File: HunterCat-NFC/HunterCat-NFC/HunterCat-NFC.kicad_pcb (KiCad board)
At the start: 2 copper layers, 80.7 x 33.5 mm, 64 parts, among them J1 Battery, J2 Conn_01x06_Female, P1 USB_C_Plug_USB2.0, Q1 DMG3415U-7, SW1 RESET, SW2 GPIO, SW3 GPIO1, SW4 GPIO2, U1 ATSAMD21E18A, U2 PN7150B0HN_C11002E-PN7150B0HN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

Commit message: add logos and mounitng holes again
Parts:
- added G***: LOGO, Aesthetics:electronic_cats_logo_4x3, F.Cu at (127.3, 105.0)
- added G***: LOGO, Aesthetics:electronic_cats_logo_4x3, B.Cu at (91.2, 92.2)
- added H1: MountingHole, MountingHole:MountingHole_2.2mm_M2, F.Cu at (83.0, 78.4)
- added H2: MountingHole, MountingHole:MountingHole_2.2mm_M2, F.Cu at (83.0, 106.1)
- added H3: MountingHole, MountingHole:MountingHole_2.2mm_M2, F.Cu at (155.8, 78.1)
- added H4: MountingHole, MountingHole:MountingHole_2.2mm_M2, F.Cu at (156.2, 106.5)

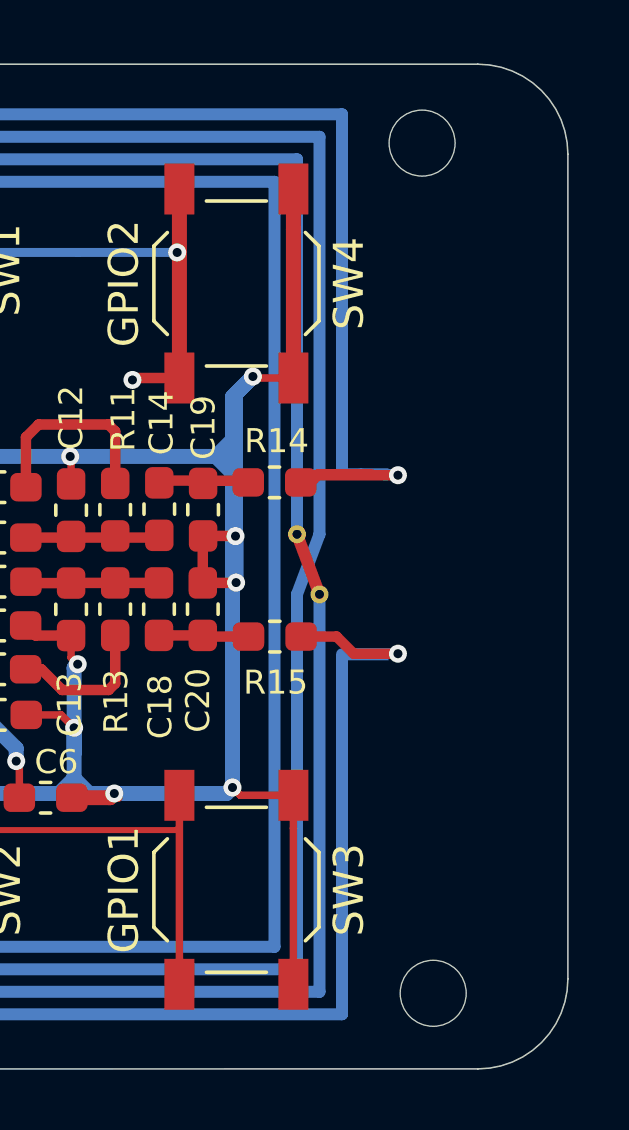
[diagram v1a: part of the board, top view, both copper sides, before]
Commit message: Accommodated screw holes
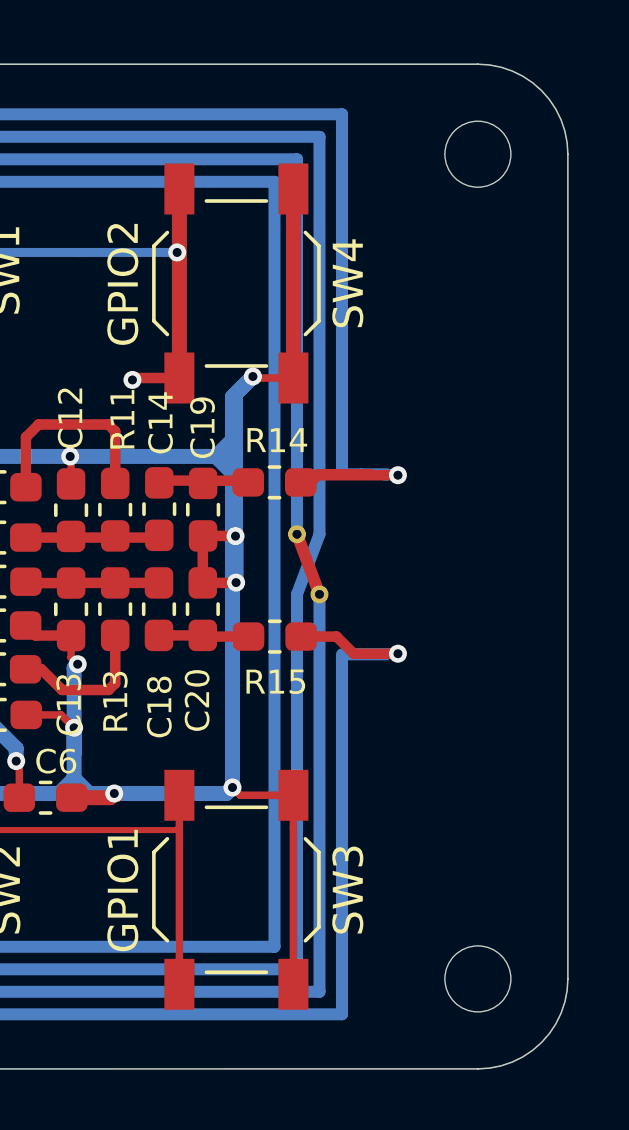
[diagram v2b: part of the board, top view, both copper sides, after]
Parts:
- moved H3 1.90 mm to (157.7, 78.5)
- moved H4 1.57 mm to (157.7, 106.0)
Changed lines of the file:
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@@
-(kicad_pcb (version 20171130) (host pcbnew "(5.1.5-0-10_14)")
+(kicad_pcb (version 20171130) (host pcbnew "(5.1.5)-3")
   (general
     (thickness 1.6)
@@
   )
   (layers
-    (0 F.Cu signal hide)
-    (31 B.Cu signal hide)
+    (0 F.Cu signal)
+    (31 B.Cu signal)
     (32 B.Adhes user)
     (33 F.Adhes user)
@@
   )
   (module MountingHole:MountingHole_2.2mm_M2 (layer F.Cu)
-    (at 156.2 106.47)
+    (at 157.69 105.99)
     (descr "Mounting Hole 2.2mm, no annular, M2")
     (tags "mounting hole 2.2mm no annular m2")
@@
   )
   (module MountingHole:MountingHole_2.2mm_M2 (layer F.Cu)
-    (at 155.83 78.13)
+    (at 157.69 78.5)
     (descr "Mounting Hole 2.2mm, no annular, M2")
     (tags "mounting hole 2.2mm no annular m2")

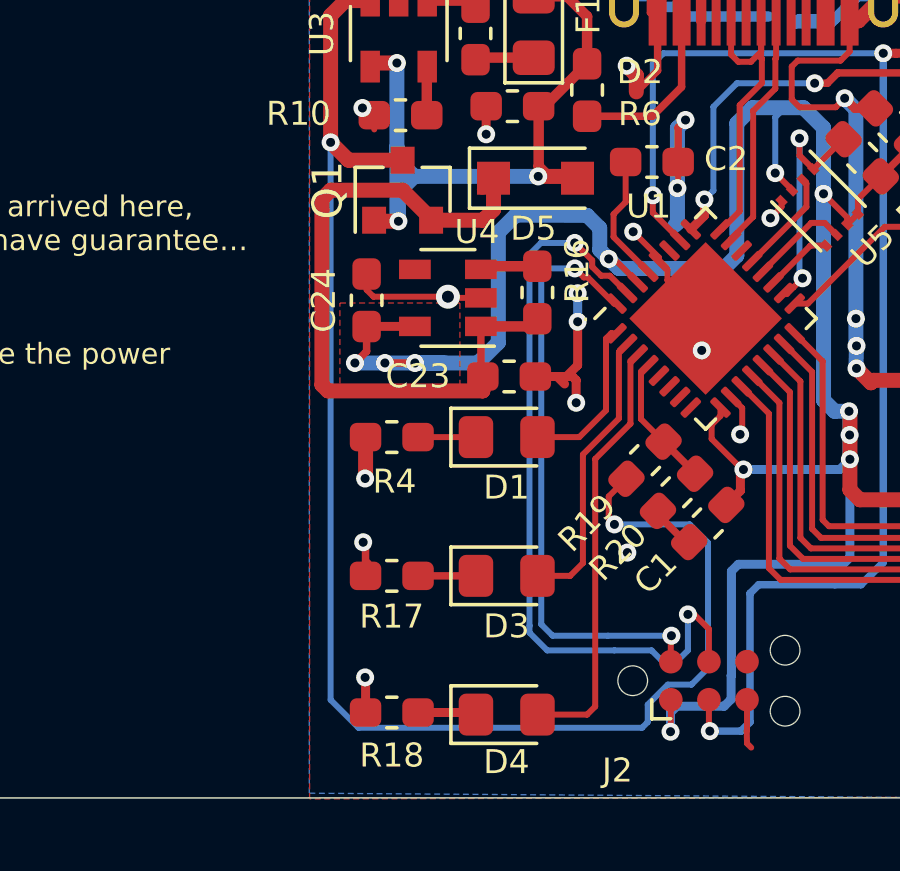
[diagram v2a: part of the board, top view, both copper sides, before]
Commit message: add switch on off
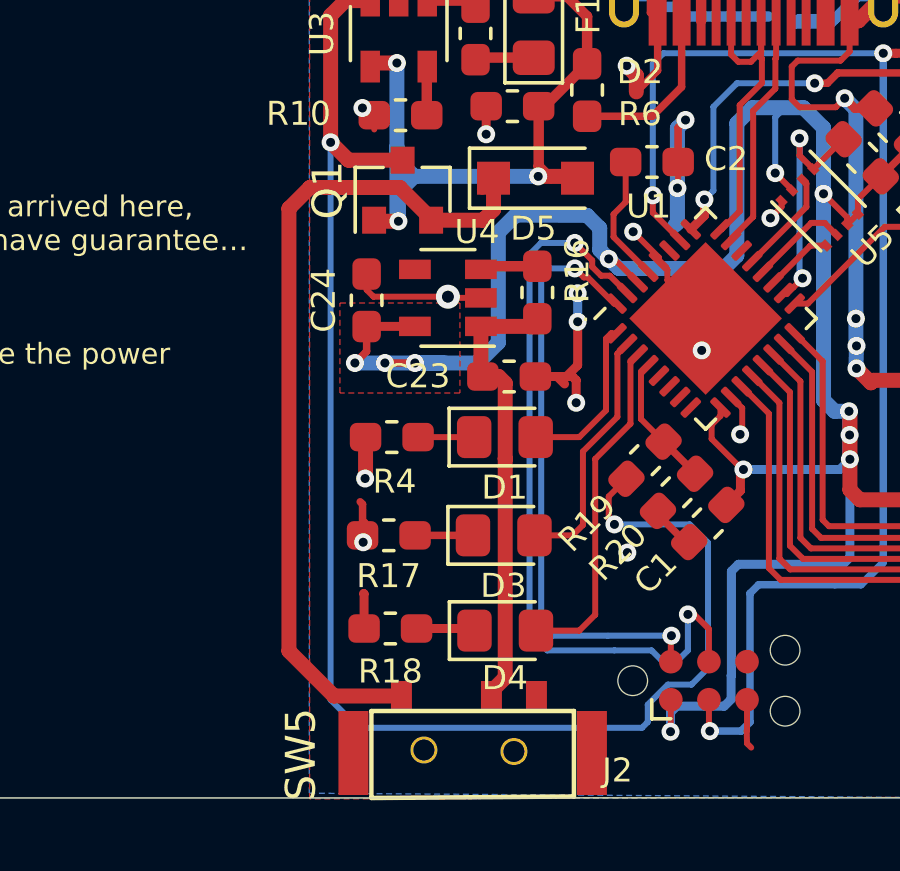
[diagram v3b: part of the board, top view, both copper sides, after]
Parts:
- added SW5: ON, hunter-cat-nfc:Micro_interruptor_SPDT, F.Cu at (104.5, 108.8)
- moved R18 2.80 mm to (105.7, 103.3)
- moved D4 2.80 mm to (109.5, 103.4)
- moved D3 1.35 mm to (109.5, 100.2)
- moved R17 1.35 mm to (105.6, 100.2)
- moved D1 0.06 mm to (109.5, 97.0)
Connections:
- D5 pad 1: Net-(C23-Pad1) -> Net-(D5-Pad1)
- Q1 pad 2: Net-(C23-Pad1) -> Net-(D5-Pad1)
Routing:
- net Net-(D5-Pad1): track 0.00 -> 28.4 mm
- net Net-(C23-Pad1): track 23.5 -> 15.1 mm
- net /LED3: track 14.4 -> 11.5 mm
- net /LED2: track 9.61 -> 8.40 mm
- net GND: vias 43 -> 42

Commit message: update traces
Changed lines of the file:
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@@
     (tags "tag connect programming header pogo pins")
     (attr virtual)
-    (fp_text reference J2 (at -3.05 2.99) (layer F.SilkS)
+    (fp_text reference J2 (at 4.25 -0.115) (layer F.SilkS)
       (effects (font (size 0.8 0.8) (thickness 0.12)))
     )
@@
     (tags "capacitor handsolder")
     (attr smd)
-    (fp_text reference C16 (at -3.15 -0.04) (layer F.SilkS)
+    (fp_text reference C16 (at -2.74 0.015) (layer F.SilkS)
       (effects (font (size 0.8 0.8) (thickness 0.12)))
     )
@@
     (tags "LED handsolder")
     (attr smd)
-    (fp_text reference D4 (at -0.01 1.58) (layer F.SilkS)
+    (fp_text reference D4 (at 2.665 -0.02) (layer F.SilkS)
       (effects (font (size 0.8 0.8) (thickness 0.12)))
     )
@@
     (tags "resistor handsolder")
     (attr smd)
-    (fp_text reference R10 (at 3.4 0.05) (layer F.SilkS)
+    (fp_text reference R10 (at 2.97 0.015) (layer F.SilkS)
       (effects (font (size 0.8 0.8) (thickness 0.12)))
     )
@@
     (tags "resistor handsolder")
     (attr smd)
-    (fp_text reference R18 (at 0 -1.43) (layer F.SilkS)
-      (effects (font (size 0.8 0.8) (thickness 0.12)))
-    )
+    (fp_text reference R18 (at -0.495 -1.2) (layer F.SilkS)
+      (effects (font (size 0.8 0.8) (thickness 0.12)))
+    )

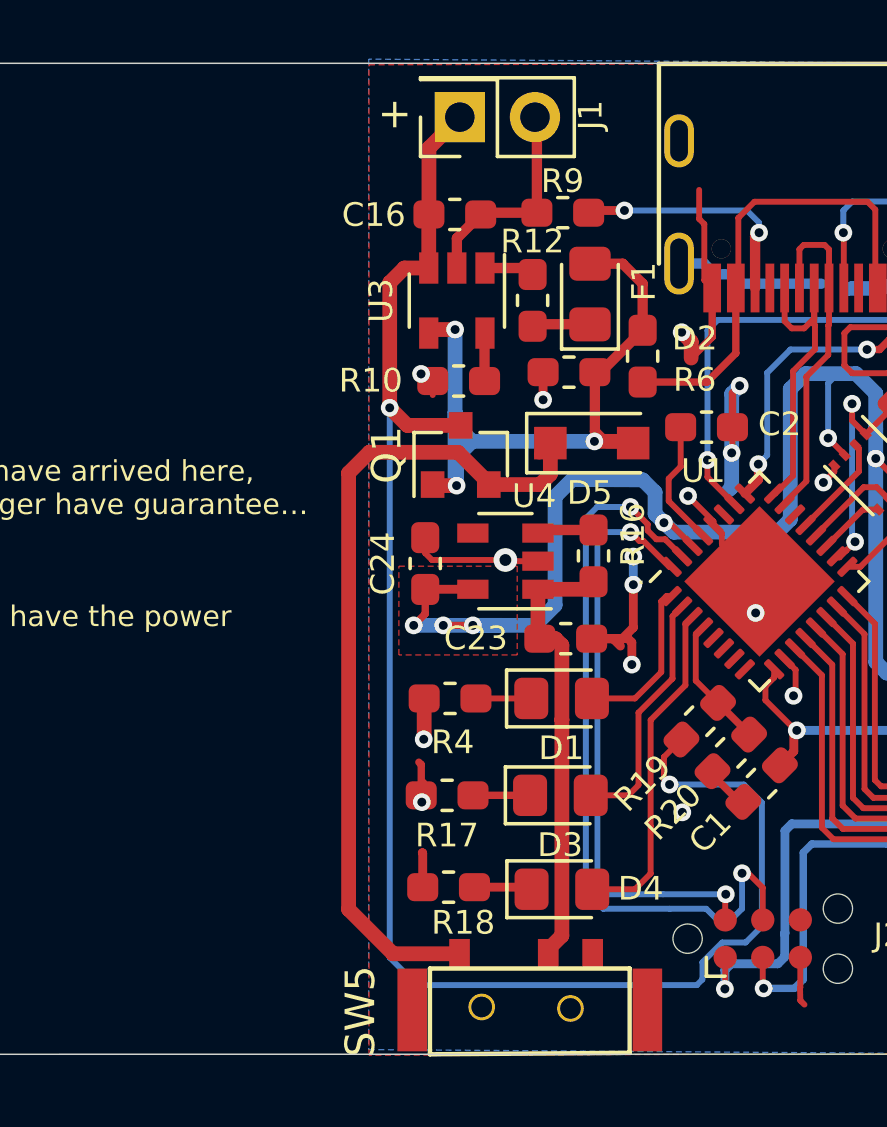
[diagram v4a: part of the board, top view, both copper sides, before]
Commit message: Moved the battery footprint
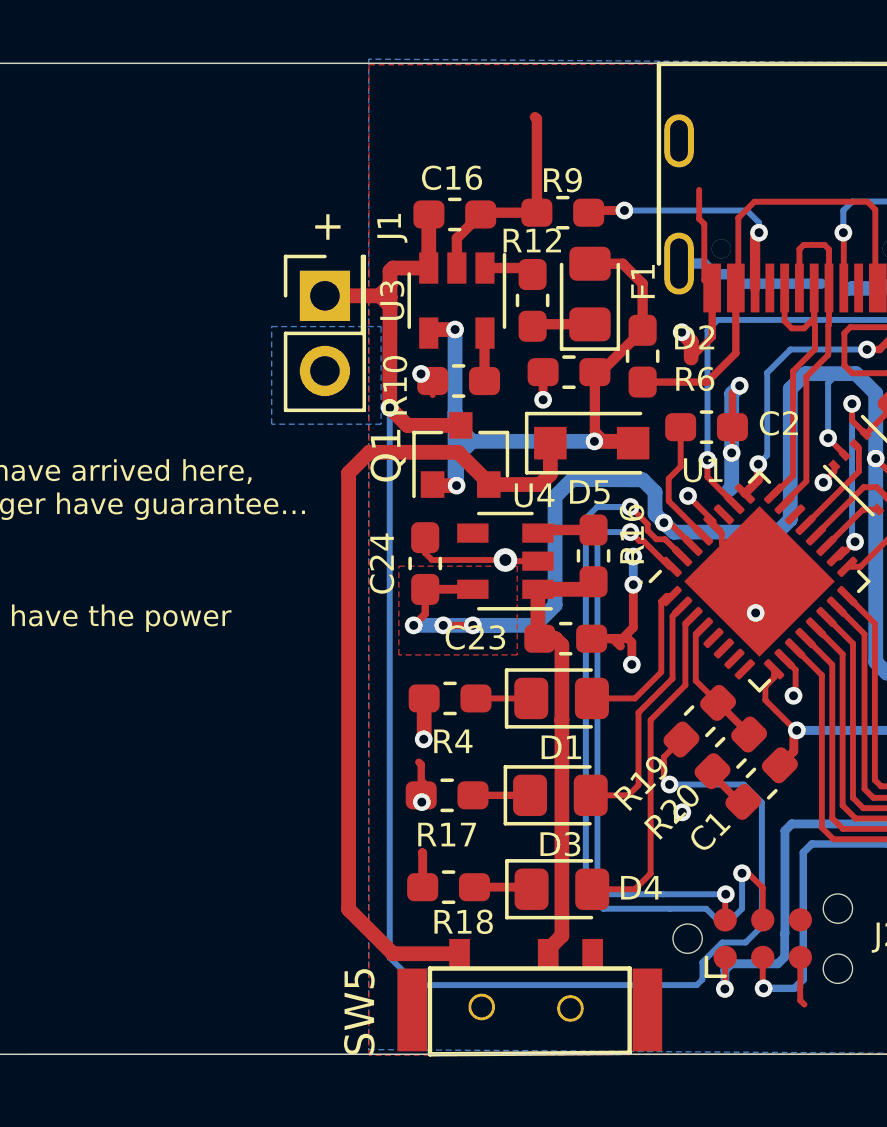
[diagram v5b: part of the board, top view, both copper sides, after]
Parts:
- moved J1 7.57 mm to (101.5, 83.4), turned to 90 degrees
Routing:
- net +BATT: track 56.0 -> 55.4 mm
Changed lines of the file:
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@@
-(kicad_pcb (version 20171130) (host pcbnew "(5.1.5-0-10_14)")
+(kicad_pcb (version 20171130) (host pcbnew "(5.1.5)-3")
   (general
     (thickness 1.6)
     (drawings 27)
-    (tracks 892)
+    (tracks 900)
     (zones 0)
     (modules 71)
@@
   )
   (module Connector_PinSocket_2.54mm:PinSocket_2x01_P2.54mm_Vertical (layer F.Cu)
-    (at 106.06 77.32 180)
+    (at 101.5 83.36 90)
     (descr "Through hole straight socket strip, 2x01, 2.54mm pitch, double cols (from Kicad 4.0.7), script generated")
     (tags "Through hole socket strip THT 2x01 2.54mm double row")
-    (fp_text reference J1 (at -4.42 0.07 90) (layer F.SilkS)
+    (fp_text reference J1 (at 2.36 2.2 90) (layer F.SilkS)
       (effects (font (size 0.8 0.8) (thickness 0.12)))
     )
-    (fp_text value Battery (at -1.27 2.77) (layer F.Fab)
+    (fp_text value Battery (at -1.27 2.77 90) (layer F.Fab)
       (effects (font (size 1 1) (thickness 0.15)))
     )
@@
     (fp_line (start 0.635 -1.27) (end 1.27 -0.635) (layer F.Fab) (width 0.1))
     (fp_line (start -3.81 -1.27) (end 0.635 -1.27) (layer F.Fab) (width 0.1))
-    (fp_text user %R (at -1.27 0) (layer F.Fab)
+    (fp_text user %R (at -1.27 0 90) (layer F.Fab)
       (effects (font (size 1 1) (thickness 0.15)))
     )
-    (pad 2 thru_hole oval (at -2.54 0 180) (size 1.7 1.7) (drill 1) (layers *.Cu *.Mask)
+    (pad 2 thru_hole oval (at -2.54 0 90) (size 1.7 1.7) (drill 1) (layers *.Cu *.Mask)
       (net 1 GND))
-    (pad 1 thru_hole rect (at 0 0 180) (size 1.7 1.7) (drill 1) (layers *.Cu *.Mask)
+    (pad 1 thru_hole rect (at 0 0 90) (size 1.7 1.7) (drill 1) (layers *.Cu *.Mask)
       (net 8 +BATT))
     (model ${KISYS3DMOD}/Connector_PinSocket_2.54mm.3dshapes/PinSocket_2x01_P2.54mm_Vertical.wrl
@@
     (tags "capacitor handsolder")
     (attr smd)
-    (fp_text reference C16 (at -2.74 0.015) (layer F.SilkS)
+    (fp_text reference C16 (at -0.09 -1.21) (layer F.SilkS)
       (effects (font (size 0.8 0.8) (thickness 0.12)))
     )
@@
     (tags "resistor handsolder")
     (attr smd)
-    (fp_text reference R10 (at 2.97 0.015) (layer F.SilkS)
+    (fp_text reference R10 (at 2.12 -0.16 90) (layer F.SilkS)
       (effects (font (size 0.8 0.8) (thickness 0.12)))
     )
@@
     (tags SOT-23-5)
     (attr smd)
-    (fp_text reference U3 (at 0 2.56 90) (layer F.SilkS)
+    (fp_text reference U3 (at 0 2.16 90) (layer F.SilkS)
       (effects (font (size 0.8 0.8) (thickness 0.12)))
     )
@@
     (arrow2b (pts (xy 80 121.04) (xy 81.126504 120.453579)))
   )
-  (gr_text + (at 103.86 77.2) (layer F.SilkS)
+  (gr_text + (at 101.6 81) (layer F.SilkS)
     (effects (font (size 1 1) (thickness 0.25)) (justify mirror))
   )
@@
   (segment (start 104.285 87.74) (end 103.69 87.145) (width 0.5) (layer F.Cu) (net 8))
   (segment (start 106.09 87.74) (end 104.285 87.74) (width 0.5) (layer F.Cu) (net 8))
-  (segment (start 104.185 82.42) (end 105.01 82.42) (width 0.5) (layer F.Cu) (net 8))
-  (segment (start 103.69 82.915) (end 104.185 82.42) (width 0.5) (layer F.Cu) (net 8))
-  (segment (start 103.69 87.145) (end 103.69 82.915) (width 0.5) (layer F.Cu) (net 8))
   (segment (start 105.01 80.615) (end 105.015 80.61) (width 0.5) (layer F.Cu) (net 8))
   (segment (start 105.01 82.42) (end 105.01 80.615) (width 0.5) (layer F.Cu) (net 8))
-  (segment (start 105.015 78.365) (end 106.06 77.32) (width 0.5) (layer F.Cu) (net 8))
-  (segment (start 105.015 80.61) (end 105.015 78.365) (width 0.5) (layer F.Cu) (net 8))
   (segment (start 104.62 106.66) (end 103.69 105.73) (width 0.2) (layer B.Cu) (net 8))
   (segment (start 114.26 105.89) (end 114.26 106.47) (width 0.2) (layer B.Cu) (net 8))
@@
   (segment (start 115.66 99.88) (end 116.27 100.49) (width 0.2) (layer B.Cu) (net 8))
   (segment (start 113.15 99.88) (end 115.66 99.88) (width 0.2) (layer B.Cu) (net 8))
+  (segment (start 103.69 87.145) (end 103.7 83.7) (width 0.5) (layer F.Cu) (net 8))
+  (segment (start 103.8 82.42) (end 105.01 82.42) (width 0.5) (layer F.Cu) (net 8))
+  (segment (start 103.7 82.52) (end 103.8 82.42) (width 0.5) (layer F.Cu) (net 8))
+  (segment (start 103.7 83.4) (end 103.66 83.36) (width 0.5) (layer F.Cu) (net 8))
+  (segment (start 103.7 83.7) (end 103.7 83.4) (width 0.5) (layer F.Cu) (net 8))
+  (segment (start 103.34 83.36) (end 101.95 83.36) (width 0.5) (layer F.Cu) (net 8))
+  (segment (start 103.66 83.36) (end 103.34 83.36) (width 0.5) (layer F.Cu) (net 8))
+  (segment (start 103.7 82.9) (end 103.7 82.52) (width 0.5) (layer F.Cu) (net 8))
+  (segment (start 103.7 83.4) (end 103.7 82.9) (width 0.5) (layer F.Cu) (net 8))
+  (segment (start 103.36 83.36) (end 103.7 83.7) (width 0.5) (layer F.Cu) (net 8))
+  (segment (start 103.34 83.36) (end 103.36 83.36) (width 0.5) (layer F.Cu) (net 8))
+  (segment (start 103.7 83) (end 103.34 83.36) (width 0.5) (layer F.Cu) (net 8))
+  (segment (start 103.7 82.9) (end 103.7 83) (width 0.5) (layer F.Cu) (net 8))
   (via (at 139.47 95.02) (size 0.6) (drill 0.3) (layers F.Cu B.Cu) (net 9))
   (segment (start 136.123903 94.150349) (end 136.123903 94.153903) (width 0.2) (layer F.Cu) (net 9))
@@
   (segment (start 124.99 85.05) (end 126.475 85.05) (width 0.25) (layer F.Cu) (net 57))
   (segment (start 124.77 84.83) (end 124.99 85.05) (width 0.25) (layer F.Cu) (net 57))
-  (segment (start 108.74 88.72) (end 109.12 88.34) (width 0.35) (layer F.Cu) (net 65))
   (segment (start 109.29 94.95) (end 108.765 94.95) (width 0.5) (layer F.Cu) (net 58))
   (segment (start 109.51001 95.17001) (end 109.29 94.95) (width 0.5) (layer F.Cu) (net 58))
@@
   (segment (start 110.325 93.28) (end 110.58 93.025) (width 0.5) (layer F.Cu) (net 58))
   (segment (start 108.7 93.28) (end 110.325 93.28) (width 0.5) (layer F.Cu) (net 58))
-  (segment (start 108.77 89.74) (end 109.12 89.39) (width 0.5) (layer F.Cu) (net 65))
-  (segment (start 109.12 89.39) (end 109.12 88.34) (width 0.5) (layer F.Cu) (net 65))
-  (segment (start 107.04 89.74) (end 108.77 89.74) (width 0.5) (layer F.Cu) (net 65))
   (segment (start 136.27 80.7) (end 136.27 85.85) (width 0.3) (layer F.Cu) (net 59))
   (segment (start 136.27 79.55) (end 136.27 80.7) (width 0.3) (layer F.Cu) (net 59))
@@
   (segment (start 118.999979 100.589979) (end 118.999979 95.471299) (width 0.2) (layer F.Cu) (net 63))
   (segment (start 147.74 100.92) (end 147.630031 101.029969) (width 0.2) (layer F.Cu) (net 63))
+  (segment (start 108.74 88.72) (end 109.12 88.34) (width 0.35) (layer F.Cu) (net 65))
+  (segment (start 108.77 89.74) (end 109.12 89.39) (width 0.5) (layer F.Cu) (net 65))
+  (segment (start 109.12 89.39) (end 109.12 88.34) (width 0.5) (layer F.Cu) (net 65))
+  (segment (start 107.04 89.74) (end 108.77 89.74) (width 0.5) (layer F.Cu) (net 65))
   (segment (start 103 88.65) (end 106 88.65) (width 0.5) (layer F.Cu) (net 65))
   (segment (start 102.3 89.35) (end 103 88.65) (width 0.5) (layer F.Cu) (net 65))
@@
     (polygon
       (pts
-        (xy 122.88 108.98) (xy 102.99 109.03) (xy 102.99 75.55) (xy 122.88 75.5)
+        (xy 122.88 108.98) (xy 102.99 109.03) (xy 102.99 82.6) (xy 102.99 75.55) (xy 122.88 75.5)
       )
     )
@@
       )
     )
+  )
+  (zone (net 1) (net_name GND) (layer B.Cu) (hatch edge 0.508)
+    (connect_pads (clearance 0.508))
+    (min_thickness 0.254)
+    (fill yes (arc_segments 32) (thermal_gap 0.508) (thermal_bridge_width 0.508))
+    (polygon
+      (pts
+        (xy 103.4 87.7) (xy 99.7 87.7) (xy 99.7 84.4) (xy 103.4 84.4)
+      )
+    )
